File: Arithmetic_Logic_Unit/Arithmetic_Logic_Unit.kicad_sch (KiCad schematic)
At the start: 1 part

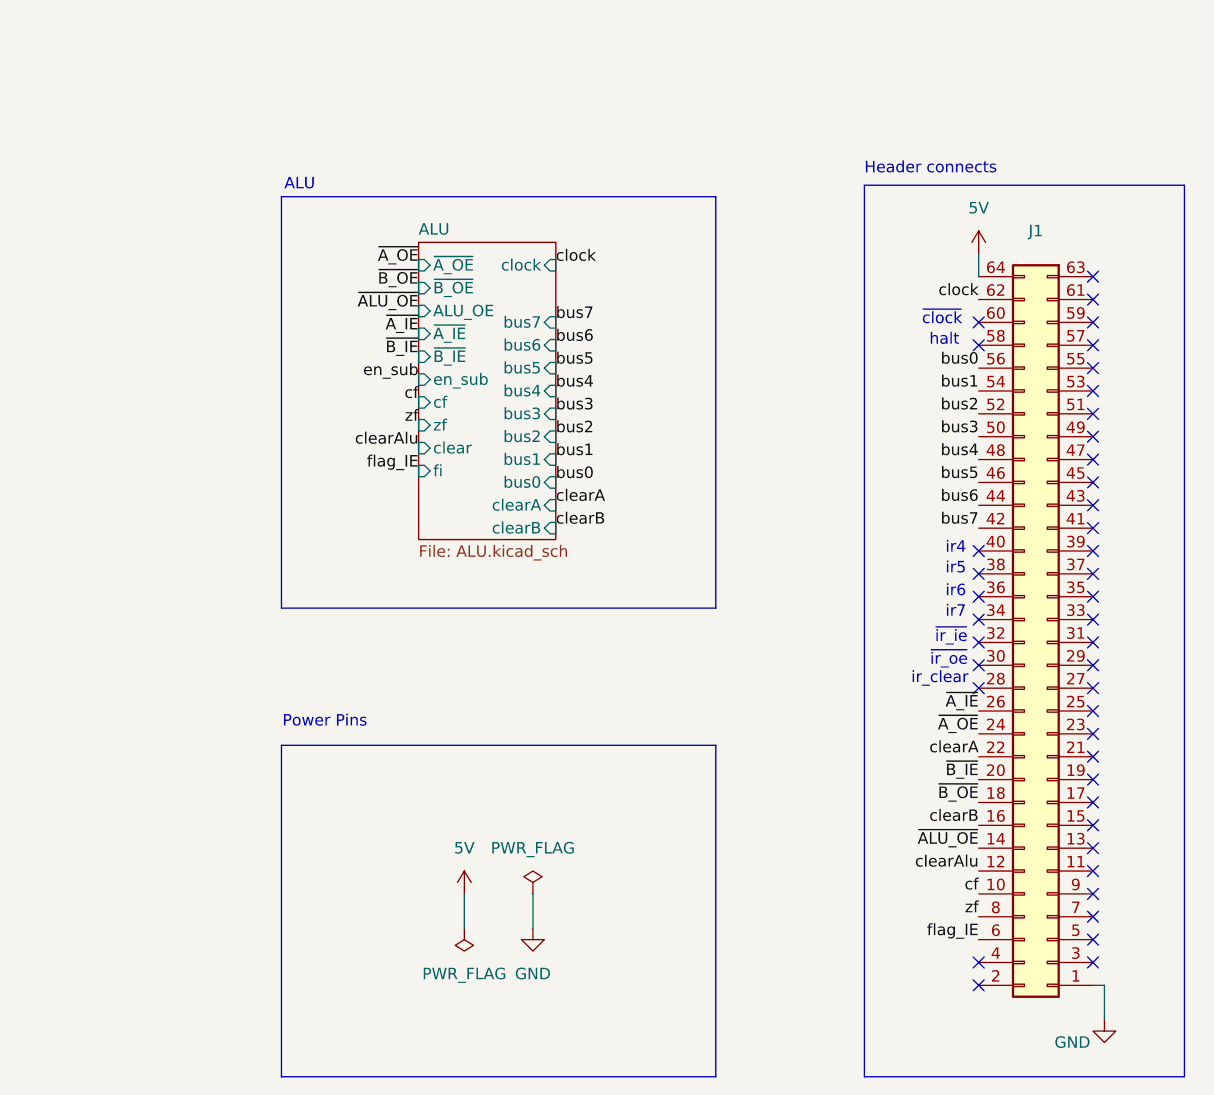
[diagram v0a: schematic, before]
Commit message: updated Arithemetic Logic Unit
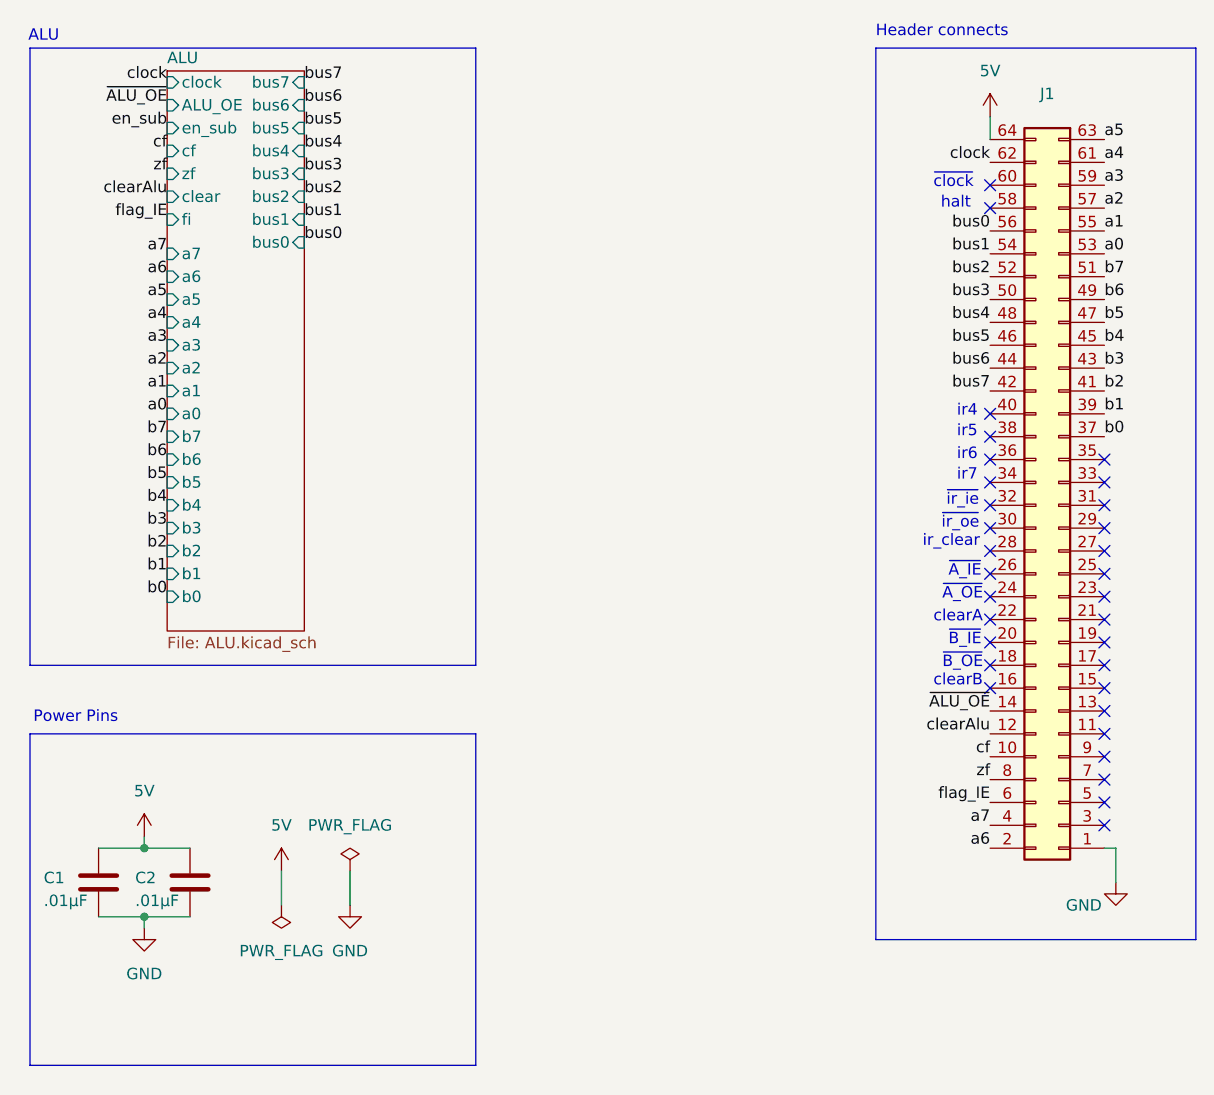
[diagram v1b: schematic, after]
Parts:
- added C1, C2: .01µF, Capacitor_THT:C_Disc_D5.0mm_W2.5mm_P2.50mm, symbol Device:C
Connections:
- net 5V: now also C1.2, C2.2
- net GND: now also C1.1, C2.1
- net a6: now reaches J1.2
- net b0: now reaches J1.37
- net b1: now reaches J1.39
- net a7: now reaches J1.4
- net b2: now reaches J1.41
- net b3: now reaches J1.43
- net b4: now reaches J1.45
- net b5: now reaches J1.47
- net b6: now reaches J1.49
- net b7: now reaches J1.51
- net a0: now reaches J1.53
- net a1: now reaches J1.55
- net a2: now reaches J1.57
- net a3: now reaches J1.59
- net a4: now reaches J1.61
- net a5: now reaches J1.63
- net clearA: no longer names the net of J1.22
- net clearB: no longer names the net of J1.16
- net ~{A_IE}: no longer names the net of J1.26
- net ~{A_OE}: no longer names the net of J1.24
- net ~{B_IE}: no longer names the net of J1.20
- net ~{B_OE}: no longer names the net of J1.18
- no-connect marks 42 -> 32
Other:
- sheet ALU ports: added a0, a1, a2, a3, a4, a5, a6, a7, b0, b1, b2, b3, b4, b5, b6, b7; removed clearA, clearB, ~{A_IE}, ~{A_OE}, ~{B_IE}, ~{B_OE}
- note added: "clearA"
- note added: "clearB"
- note added: "~{A_IE}"
- note added: "~{A_OE}"
- note added: "~{B_IE}"
- note added: "~{B_OE}"
- moved on the sheet: J1

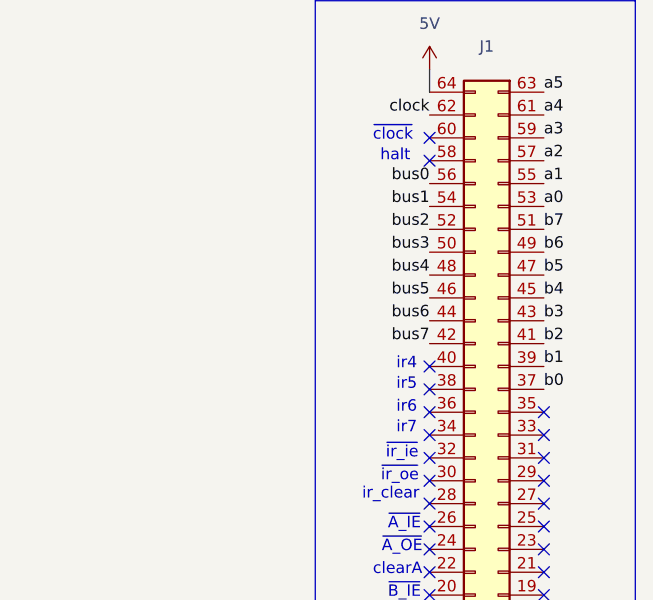
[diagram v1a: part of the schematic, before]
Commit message: updated RAM, changed bus alignment in ALU, RAM, and registers
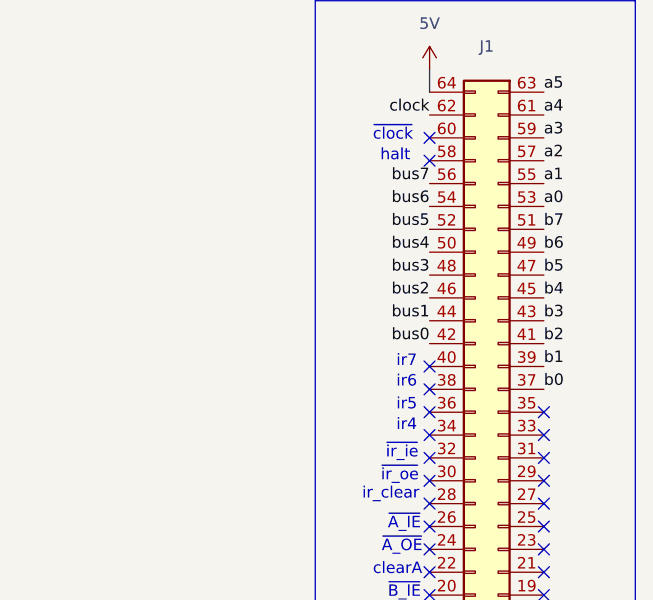
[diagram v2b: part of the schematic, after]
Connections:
- net bus0: now also J1.42; no longer J1.56
- net bus1: now also J1.44; no longer J1.54
- net bus2: now also J1.46; no longer J1.52
- net bus3: now also J1.48; no longer J1.50
- net bus4: now also J1.50; no longer J1.48
- net bus5: now also J1.52; no longer J1.46
- net bus6: now also J1.54; no longer J1.44
- net bus7: now also J1.56; no longer J1.42
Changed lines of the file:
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@@
 	(text "ir5"
 		(exclude_from_sim no)
-		(at 165.1 68.072 0)
+		(at 165.1 70.358 0)
 		(effects
 			(font
@@
 	(text "ir6"
 		(exclude_from_sim no)
-		(at 165.1 70.612 0)
+		(at 165.1 67.818 0)
 		(effects
 			(font
@@
 	(text "ir7"
 		(exclude_from_sim no)
-		(at 165.1 72.898 0)
+		(at 165.1 65.532 0)
 		(effects
 			(font
@@
 	(text "ir4"
 		(exclude_from_sim no)
-		(at 165.1 65.786 0)
+		(at 165.1 72.644 0)
 		(effects
 			(font
@@
 		)
 	)
+	(label "bus6"
+		(at 167.64 48.26 180)
+		(effects
+			(font
+				(size 1.27 1.27)
+			)
+			(justify right bottom)
+		)
+	)
 	(label "a0"
 		(at 76.2 66.04 180)
@@
 	)
 	(label "bus7"
+		(at 167.64 45.72 180)
+		(effects
+			(font
+				(size 1.27 1.27)
+			)
+			(justify right bottom)
+		)
+	)
+	(label "bus7"
 		(at 91.44 29.21 0)
 		(effects
@@
 		)
 	)
-	(label "bus5"
-		(at 167.64 58.42 180)
-		(effects
-			(font
-				(size 1.27 1.27)
-			)
-			(justify right bottom)
-		)
-	)
 	(label "b3"
 		(at 180.34 60.96 0)
@@
 		)
 	)
-	(label "bus7"
-		(at 167.64 63.5 180)
-		(effects
-			(font
-				(size 1.27 1.27)
-			)
-			(justify right bottom)
-		)
-	)
 	(label "a0"
 		(at 180.34 48.26 0)
@@
 		)
 	)
+	(label "bus4"
+		(at 167.64 53.34 180)
+		(effects
+			(font
+				(size 1.27 1.27)
+			)
+			(justify right bottom)
+		)
+	)
 	(label "a5"
 		(at 76.2 53.34 180)
@@
 		)
 	)
-	(label "bus4"
-		(at 167.64 55.88 180)
-		(effects
-			(font
-				(size 1.27 1.27)
-			)
-			(justify right bottom)
-		)
-	)
-	(label "bus3"
-		(at 167.64 53.34 180)
-		(effects
-			(font
-				(size 1.27 1.27)
-			)
-			(justify right bottom)
-		)
-	)
-	(label "bus1"
-		(at 167.64 48.26 180)
-		(effects
-			(font
-				(size 1.27 1.27)
-			)
-			(justify right bottom)
-		)
-	)
 	(label "b6"
 		(at 76.2 71.12 180)
@@
 		)
 	)
-	(label "bus6"
-		(at 167.64 60.96 180)
-		(effects
-			(font
-				(size 1.27 1.27)
-			)
-			(justify right bottom)
-		)
-	)
 	(label "a6"
 		(at 167.64 114.3 180)
@@
 		)
 	)
+	(label "bus3"
+		(at 167.64 55.88 180)
+		(effects
+			(font
+				(size 1.27 1.27)
+			)
+			(justify right bottom)
+		)
+	)
 	(label "bus0"
-		(at 167.64 45.72 180)
+		(at 167.64 63.5 180)
+		(effects
+			(font
+				(size 1.27 1.27)
+			)
+			(justify right bottom)
+		)
+	)
+	(label "bus1"
+		(at 167.64 60.96 180)
+		(effects
+			(font
+				(size 1.27 1.27)
+			)
+			(justify right bottom)
+		)
+	)
+	(label "bus2"
+		(at 167.64 58.42 180)
 		(effects
 			(font
@@
 		)
 	)
-	(label "bus2"
-		(at 167.64 50.8 180)
-		(effects
-			(font
-				(size 1.27 1.27)
-			)
-			(justify right bottom)
-		)
-	)
 	(label "~{ALU_OE}"
 		(at 76.2 31.75 180)
@@
 		)
 	)
+	(label "bus5"
+		(at 167.64 50.8 180)
+		(effects
+			(font
+				(size 1.27 1.27)
+			)
+			(justify right bottom)
+		)
+	)
